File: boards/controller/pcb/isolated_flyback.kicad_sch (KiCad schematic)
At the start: 20 parts, among them T901 150u

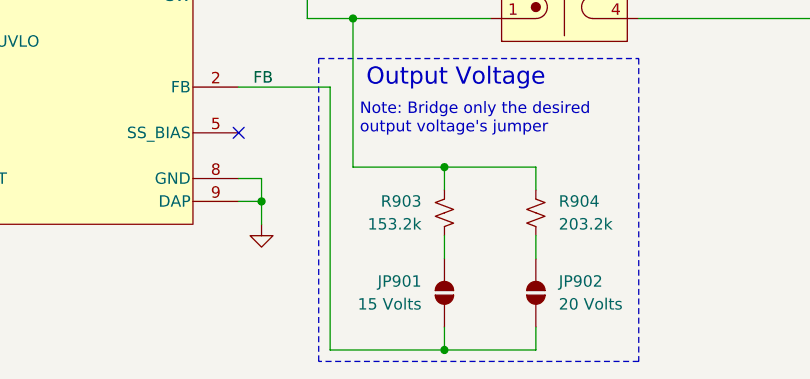
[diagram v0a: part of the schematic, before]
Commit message: controller: pcb: Update schematic
Signed-off-by: Nicholas Loehrke <nicholasnloehrke@gmail.com>
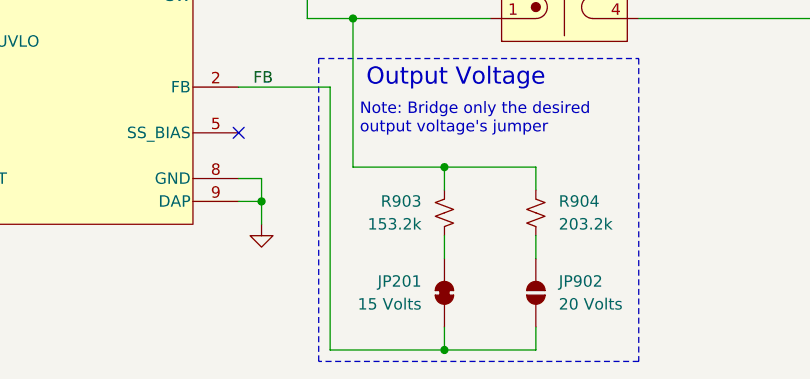
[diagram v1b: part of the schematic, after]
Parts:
- removed JP901: 15 Volts, Jumper:SolderJumper-2_P1.3mm_Open_RoundedPad1.0x1.5mm, symbol Jumper:SolderJumper_2_Open
- added JP201: 15 Volts, symbol Jumper:SolderJumper_2_Bridged
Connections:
- net FB: now also JP201.1 (A)
- net at R903.2: now also JP201.2 (B)
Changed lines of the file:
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@@
 	)
 	(symbol
-		(lib_id "Jumper:SolderJumper_2_Open")
+		(lib_id "Jumper:SolderJumper_2_Bridged")
 		(at 142.24 119.38 270)
 		(mirror x)
@@
 		(on_board yes)
 		(dnp no)
-		(property "Reference" "JP901"
+		(property "Reference" "JP201"
 			(at 139.7 118.1099 90)
 			(effects
@@
 			)
 		)
-		(property "Footprint" "Jumper:SolderJumper-2_P1.3mm_Open_RoundedPad1.0x1.5mm"
+		(property "Footprint" ""
 			(at 142.24 119.38 0)
 			(effects
@@
 			)
 		)
-		(property "Description" "Solder Jumper, 2-pole, open"
+		(property "Description" "Solder Jumper, 2-pole, closed/bridged"
 			(at 142.24 119.38 0)
 			(effects
@@
 			)
 		)
+		(pin "1"
+		)
 		(pin "2"
 		)
-		(pin "1"
-		)
 		(instances
-			(project "controller"
+			(project ""
 				(path "/5caba13a-97ae-46d4-856f-900b12012fd8/3c6b0707-a67d-4a65-a38c-f4ab92a2c5a4"
-					(reference "JP901")
+					(reference "JP201")
 					(unit 1)
 				)

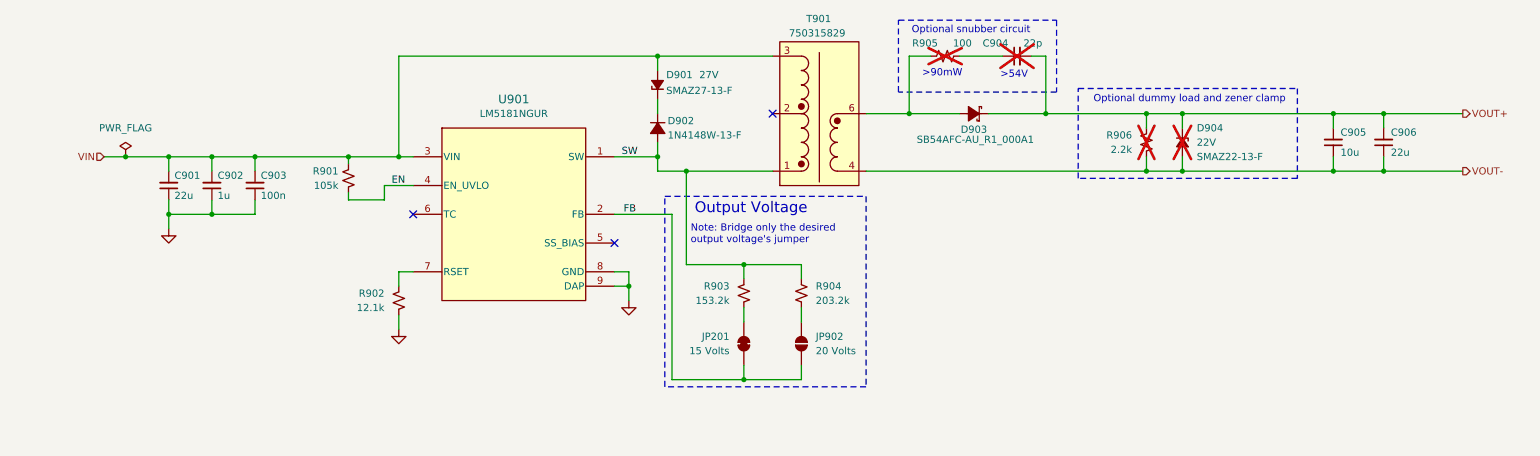
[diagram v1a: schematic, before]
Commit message: controller: pcb: Update schematic
Signed-off-by: Nicholas Loehrke <nicholasnloehrke@gmail.com>
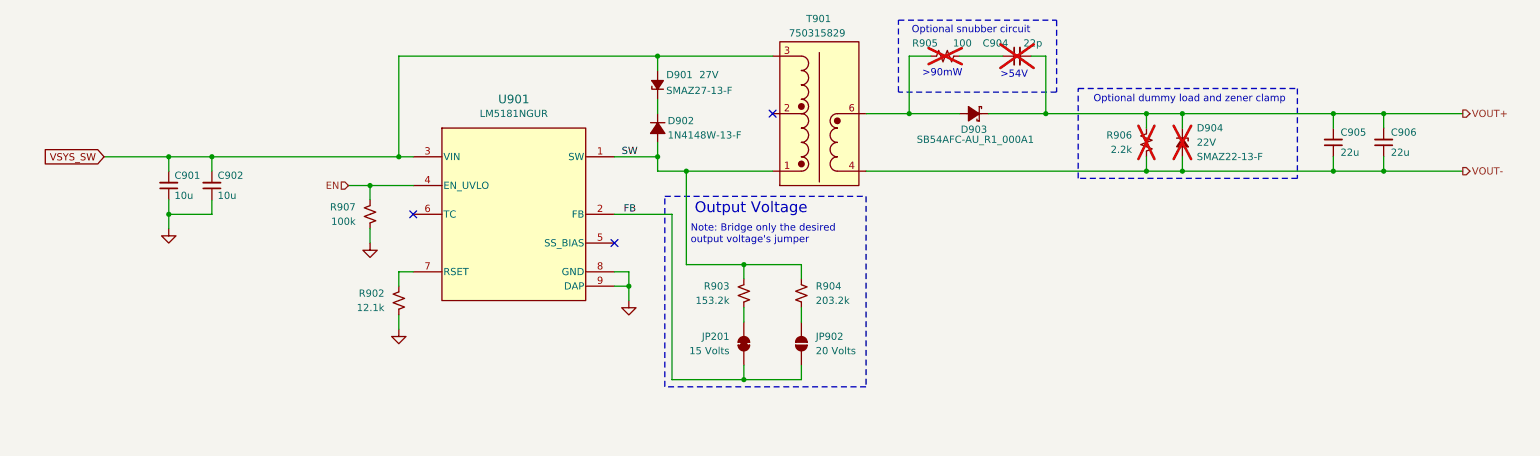
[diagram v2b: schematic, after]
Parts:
- removed C903: 100n, Capacitor_SMD:C_0603_1608Metric, symbol Device:C_Small
- removed R901: 105k, symbol Device:R_Small_US
- added R907: 100k, Resistor_SMD:R_0603_1608Metric, symbol Device:R_Small_US
- C901: value 22u -> 10u
- C902: value 1u -> 10u; footprint Capacitor_SMD:C_0603_1608Metric -> Capacitor_SMD:C_1206_3216Metric
- C905: value 10u -> 22u
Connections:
- net EN: now also R907.1
- net GND: now also R907.2
- net VIN renamed VSYS_SW

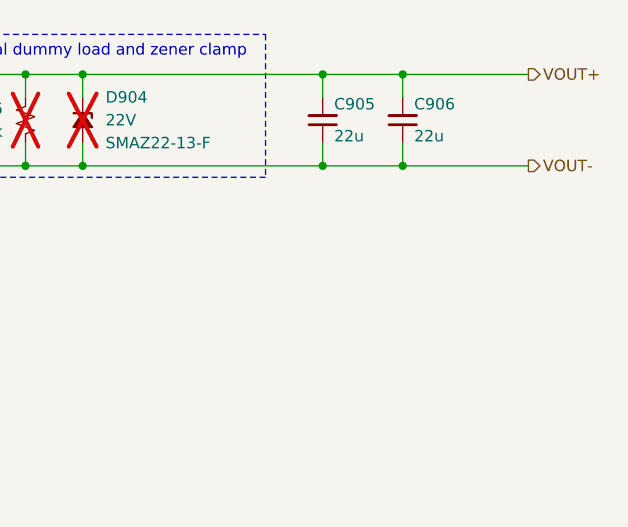
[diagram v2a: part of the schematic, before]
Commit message: controller: pcb: Update schematic
Signed-off-by: Nicholas Loehrke <nicholasnloehrke@gmail.com>
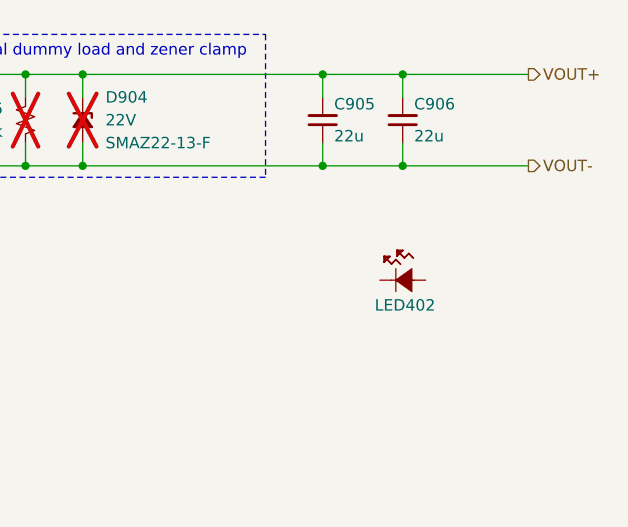
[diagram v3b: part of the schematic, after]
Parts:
- added LED402: B1911PG--20D000514U1930, LED_B1911PG--20D000514U1930_HVK, symbol B1911PG--20D000514U1930:B1911PG--20D000514U1930
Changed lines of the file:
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@@
+		)
+	)
+	(symbol
+		(lib_id "B1911PG--20D000514U1930:B1911PG--20D000514U1930")
+		(at 257.81 101.6 0)
+		(mirror y)
+		(unit 1)
+		(exclude_from_sim no)
+		(in_bom yes)
+		(on_board yes)
+		(dnp no)
+		(property "Reference" "LED402"
+			(at 255.524 104.394 0)
+			(effects
+				(font
+					(size 1.27 1.27)
+				)
+			)
+		)
+		(property "Value" "B1911PG--20D000514U1930"
+			(at 254.8255 96.52 0)
+			(effects
+				(font
+					(size 1.524 1.524)
+				)
+				(hide yes)
+			)
+		)
+		(property "Footprint" "LED_B1911PG--20D000514U1930_HVK"
+			(at 255.016 91.186 0)
+			(effects
+				(font
+					(size 1.27 1.27)
+					(italic yes)
+				)
+				(hide yes)
+			)
+		)
+		(property "Datasheet" "B1911PG--20D000514U1930"
+			(at 255.524 94.488 0)
+			(effects
+				(font
+					(size 1.27 1.27)
+					(italic yes)
+				)
+				(hide yes)
+			)
+		)
+		(property "Description" ""
+			(at 257.81 101.6 0)
+			(effects
+				(font
+					(size 1.27 1.27)
+				)
+				(hide yes)
+			)
+		)
+		(pin "1"
+		)
+		(pin "2"
+		)
+		(instances
+			(project "controller"
+				(path "/5caba13a-97ae-46d4-856f-900b12012fd8/3c6b0707-a67d-4a65-a38c-f4ab92a2c5a4"
+					(reference "LED402")
+					(unit 1)
+				)
+			)
 		)
 	)

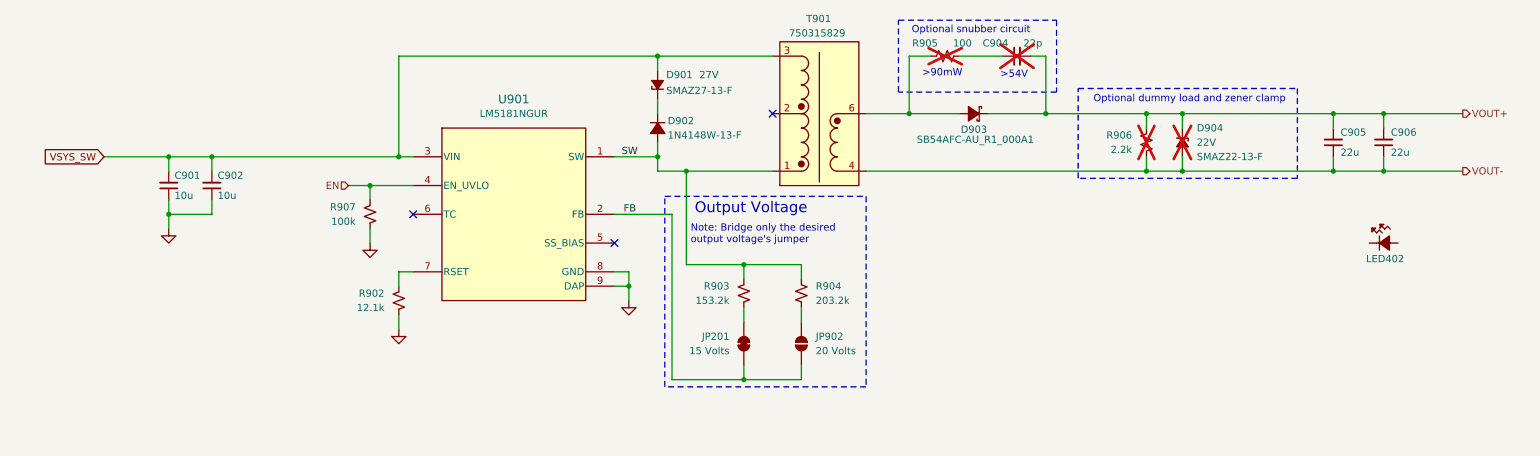
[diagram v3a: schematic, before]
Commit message: controller: pcb: Update schematic
Signed-off-by: Nicholas Loehrke <nicholasnloehrke@gmail.com>
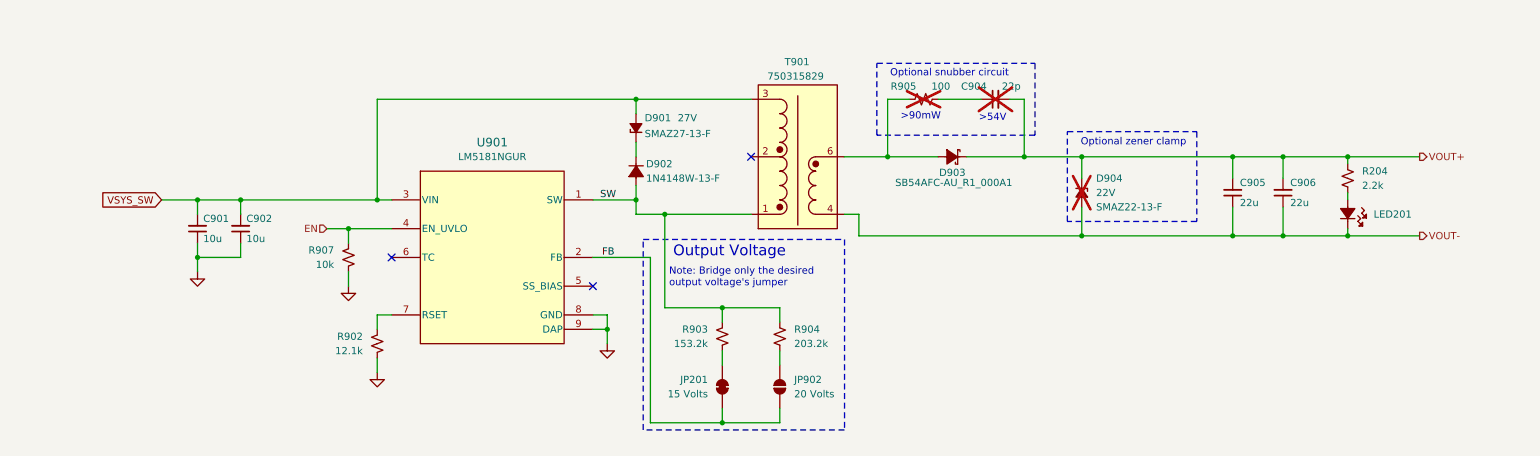
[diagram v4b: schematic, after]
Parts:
- removed LED402: B1911PG--20D000514U1930, LED_B1911PG--20D000514U1930_HVK, symbol B1911PG--20D000514U1930:B1911PG--20D000514U1930
- removed R906: 2.2k, Resistor_SMD:R_0603_1608Metric, symbol Device:R_Small_US
- added LED201: B1911PG--20D000514U1930, LED_B1911PG--20D000514U1930_HVK, symbol B1911PG--20D000514U1930:B1911PG--20D000514U1930
- added R204: 2.2k, symbol Device:R_Small_US
- R907: value 100k -> 10k
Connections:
- net VOUT+: now also R204.1
- net VOUT-: now also LED201.1
- new net: LED201.2, R204.2
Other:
- note added: "Optional zener clamp"
- note removed: "Optional dummy load and zener clamp"
- moved on the sheet: C901, C902, C904, C905, C906, D901, D902, D903, D904, JP201, JP902, R902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
